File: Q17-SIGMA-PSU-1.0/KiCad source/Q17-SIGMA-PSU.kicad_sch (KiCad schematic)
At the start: 80 parts, among them J1-1 V+ (IN), J1-2 GND, J1-3 V- (IN), J2-1 V+, J2-2 V+, J2-3 GND, J2-4 GND, J2-5 GND, J2-6 V-, J2-7 V-, Q1 BC548B, Q2 BC558B, Q3 BC548B, Q4 BC556B, Q5 BC546B, Q6 IRFZ24NPBF, Q7 IRF9Z34NPBF, Q8 IRFZ24NPBF, Q9 IRF9Z34NPBF, U1 ZHB6792TA, U2 ZHB6792TA

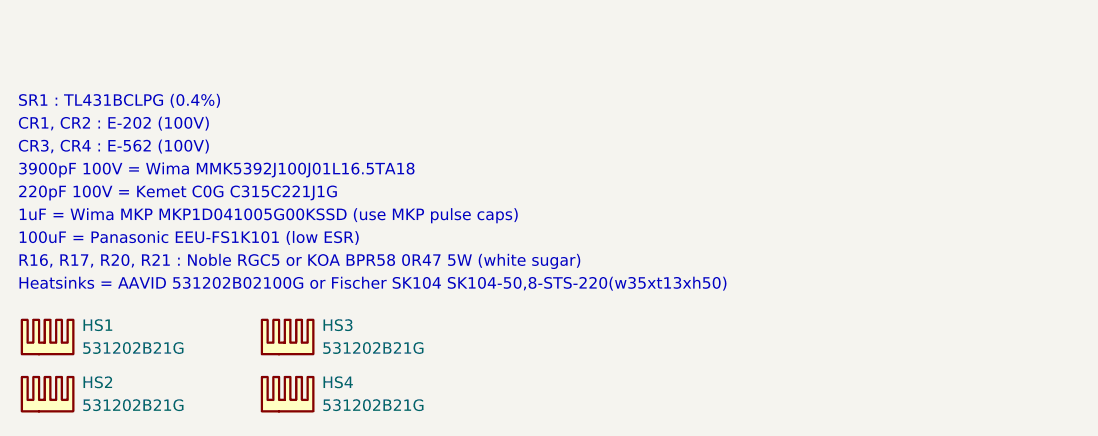
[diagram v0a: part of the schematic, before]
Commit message: Update Q17-SIGMA-PSU.kicad_sch
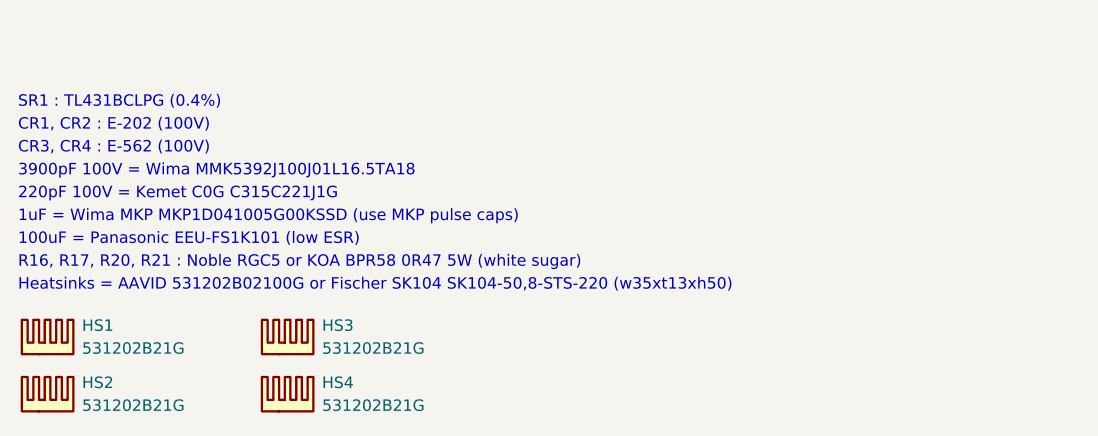
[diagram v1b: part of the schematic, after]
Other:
- note added: "Heatsinks = AAVID 531202B02100G or Fischer SK104 SK104-50,8-STS-220 (w35xt13xh50)"
- note removed: "Heatsinks = AAVID 531202B02100G or Fischer SK104 SK104-50,8-STS-220(w35xt13xh50)"
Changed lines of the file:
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@@
 		(title "Q17-SIGMA Power Supply")
 		(date "2024-04-14")
-		(rev "1.0")
+		(rev "1.0.1")
 		(company "PCB and BOM by stef")
 		(comment 2 "Design and test by Moor")
@@
 		)
 	)
-	(text "Heatsinks = AAVID 531202B02100G or Fischer SK104 SK104-50,8-STS-220(w35xt13xh50)"
+	(text "Heatsinks = AAVID 531202B02100G or Fischer SK104 SK104-50,8-STS-220 (w35xt13xh50)"
 		(exclude_from_sim no)
 		(at 14.478 181.61 0)

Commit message: Q17-SIGMA-PSU-schematic update
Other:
- note added: "All capacitors rated for 80V/100V minimum."
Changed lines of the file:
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@@
 	(title_block
 		(title "Q17-SIGMA Power Supply")
-		(date "2024-04-14")
-		(rev "1.0.1")
+		(date "2024-04-15")
+		(rev "1.0.2")
 		(company "PCB and BOM by stef")
 		(comment 2 "Design and test by Moor")
@@
 		)
 	)
+	(text "All capacitors rated for 80V/100V minimum."
+		(exclude_from_sim no)
+		(at 14.732 158.75 0)
+		(effects
+			(font
+				(size 1.27 1.27)
+			)
+			(justify left)
+		)
+	)
 	(text "1uF = Wima MKP MKP1D041005G00KSSD (use MKP pulse caps)"
 		(exclude_from_sim no)
@@
 		(dnp no)
 		(property "Reference" "R4"
-			(at 110.49 70.358 0)
+			(at 110.49 70.104 0)
 			(effects
 				(font
@@
 		(dnp no)
 		(property "Reference" "R6"
-			(at 119.38 70.358 0)
+			(at 119.38 70.104 0)
 			(effects
 				(font
@@
 		)
 		(property "Value" "510K"
-			(at 119.38 72.136 0)
+			(at 119.38 72.39 0)
 			(effects
 				(font
@@
 		)
 		(property "Value" "100R"
-			(at 215.138 121.158 0)
+			(at 215.138 121.412 0)
 			(effects
 				(font
@@
 		)
 		(property "Value" "100R"
-			(at 202.438 121.158 0)
+			(at 202.438 121.412 0)
 			(effects
 				(font

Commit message: Update Q17-SIGMA-PSU diagram
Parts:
- removed Q6, Q8: IRFZ24NPBF, Package_TO_SOT_THT:TO-220-3_Vertical, symbol Transistor_FET:IRF9540N
- added Q6, Q8: IRFZ24NPBF, Package_TO_SOT_THT:TO-220-3_Vertical, symbol Transistor_FET:IRF540N
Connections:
- net V+ (IN): now also Q6.2 (D), Q8.2 (D)
- net at R10.1: now also Q6.1 (G)
- net at R16.1: now also Q6.3 (S)
- net at R13.1: now also Q8.1 (G)
- net at R17.1: now also Q8.3 (S)
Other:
- note added: "100uF = Panasonic EEU-FS1K101 (low ESR, miniature)"
- note added: "CR1, CR2 : Semitec E-202 (100V)"
- note added: "CR3, CR4 : Semitec E-562 (100V)"
- note added: "Q6, Q8 : IRFZ24NPBF or IRF530NPBF"
- note added: "Q7, Q9 : IRF9Z34NPBF or IRF9540NPBF"
- note removed: "100uF = Panasonic EEU-FS1K101 (low ESR)"
- note removed: "CR1, CR2 : E-202 (100V)"
- note removed: "CR3, CR4 : E-562 (100V)"
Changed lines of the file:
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@@
 		(title "Q17-SIGMA Power Supply")
 		(date "2024-04-15")
-		(rev "1.0.2")
+		(rev "1.0.3")
 		(company "PCB and BOM by stef")
 		(comment 2 "Design and test by Moor")
@@
 		)
 	)
-	(text "100uF = Panasonic EEU-FS1K101 (low ESR)"
+	(text "100uF = Panasonic EEU-FS1K101 (low ESR, miniature)"
 		(exclude_from_sim no)
 		(at 14.478 176.53 0)
@@
 		)
 	)
-	(text "CR3, CR4 : E-562 (100V)"
+	(text "CR3, CR4 : Semitec E-562 (100V)"
 		(exclude_from_sim no)
 		(at 14.478 166.37 0)
@@
 		)
 	)
-	(text "CR1, CR2 : E-202 (100V)"
+	(text "Q7, Q9 : IRF9Z34NPBF or IRF9540NPBF"
+		(exclude_from_sim no)
+		(at 14.732 156.21 0)
+		(effects
+			(font
+				(size 1.27 1.27)
+			)
+			(justify left)
+		)
+	)
+	(text "CR1, CR2 : Semitec E-202 (100V)"
 		(exclude_from_sim no)
 		(at 14.478 163.83 0)
@@
 		)
 	)
+	(text "Q6, Q8 : IRFZ24NPBF or IRF530NPBF"
+		(exclude_from_sim no)
+		(at 14.732 153.67 0)
+		(effects
+			(font
+				(size 1.27 1.27)
+			)
+			(justify left)
+		)
+	)
 	(text "220pF 100V = Kemet C0G C315C221J1G "
 		(exclude_from_sim no)
@@
 	)
 	(symbol
+		(lib_id "Transistor_FET:IRF540N")
+		(at 213.36 53.34 90)
+		(unit 1)
+		(exclude_from_sim no)
+		(in_bom yes)
+		(on_board yes)
+		(dnp no)
+		(fields_autoplaced yes)
+		(property "Reference" "Q8"
+			(at 213.36 44.45 90)
+			(effects
+				(font
+					(size 1.27 1.27)
+				)
+			)
+		)
+		(property "Value" "IRFZ24NPBF"
+			(at 213.36 46.99 90)
+			(effects
+				(font
+					(size 1.27 1.27)
+				)
+			)
+		)
+		(property "Footprint" "Package_TO_SOT_THT:TO-220-3_Vertical"
+			(at 215.265 48.26 0)
+			(effects
+				(font
+					(size 1.27 1.27)
+					(italic yes)
+				)
+				(justify left)
+				(hide yes)
+			)
+		)
+		(property "Datasheet" "https://www.mouser.fr/datasheet/2/196/Infineon_IRFZ24N_DataSheet_v01_01_EN-3363353.pdf"
+			(at 217.17 48.26 0)
+			(effects
+				(font
+					(size 1.27 1.27)
+				)
+				(justify left)
+				(hide yes)
+			)
+		)
+		(property "Description" "MOSFET MOSFT 55V 17A 70mOhm 13.3nC"
+			(at 213.36 53.34 0)
+			(effects
+				(font
+					(size 1.27 1.27)
+				)
+				(hide yes)
+			)
+		)
+		(property "Part#" "IRFZ24NPBF"
+			(at 213.36 53.34 0)
+			(effects
+				(font
+					(size 1.27 1.27)
+				)
+				(hide yes)
+			)
+		)
+		(property "Mouser" "942-IRFZ24NPBF"
+			(at 213.36 53.34 0)
+			(effects
+				(font
+					(size 1.27 1.27)
+				)
+				(hide yes)
+			)
+		)
+		(pin "1"
+		)
+		(pin "2"
+		)
+		(pin "3"
+		)
+		(instances
+			(project "Q17-SIGMA-PSU"
+				(path "/6f6e3082-536f-4dd6-9db0-4603443bd8a6"
+					(reference "Q8")
+					(unit 1)
+				)
+			)
+		)
+	)
+	(symbol
 		(lib_id "Device:C_Polarized")
 		(at 96.52 78.74 0)
@@
 	)
 	(symbol
-		(lib_id "Transistor_FET:IRF9540N")
-		(at 200.66 41.91 90)
-		(unit 1)
-		(exclude_from_sim no)
-		(in_bom yes)
-		(on_board yes)
-		(dnp no)
-		(fields_autoplaced yes)
-		(property "Reference" "Q6"
-			(at 200.66 33.02 90)
-			(effects
-				(font
-					(size 1.27 1.27)
-				)
-			)
-		)
-		(property "Value" "IRFZ24NPBF"
-			(at 200.66 35.56 90)
-			(effects
-				(font
-					(size 1.27 1.27)
-				)
-			)
-		)
-		(property "Footprint" "Package_TO_SOT_THT:TO-220-3_Vertical"
-			(at 202.565 36.83 0)
-			(effects
-				(font
-					(size 1.27 1.27)
-					(italic yes)
-				)
-				(justify left)
-				(hide yes)
-			)
-		)
-		(property "Datasheet" "https://www.mouser.fr/datasheet/2/196/Infineon_IRFZ24N_DataSheet_v01_01_EN-3363353.pdf"
-			(at 204.47 36.83 0)
-			(effects
-				(font
-					(size 1.27 1.27)
-				)
-				(justify left)
-				(hide yes)
-			)
-		)
-		(property "Description" "MOSFET MOSFT 55V 17A 70mOhm 13.3nC"
-			(at 200.66 41.91 0)
-			(effects
-				(font
-					(size 1.27 1.27)
-				)
-				(hide yes)
-			)
-		)
-		(property "Part#" "IRFZ24NPBF"
-			(at 200.66 41.91 90)
-			(effects
-				(font
-					(size 1.27 1.27)
-				)
-				(hide yes)
-			)
-		)
-		(property "Mouser" "942-IRFZ24NPBF"
-			(at 200.66 41.91 90)
-			(effects
-				(font
-					(size 1.27 1.27)
-				)
-				(hide yes)
-			)
-		)
-		(pin "2"
-		)
-		(pin "1"
-		)
-		(pin "3"
-		)
-		(instances
-			(project "Q17-SIGMA-PSU"
-				(path "/6f6e3082-536f-4dd6-9db0-4603443bd8a6"
-					(reference "Q6")
-					(unit 1)
-				)
-			)
-		)
-	)
-	(symbol
 		(lib_id "Device:C_Polarized")
 		(at 96.52 105.41 0)
@@
 			)
 		)
-		(property "Datasheet" "https://www.mouser.fr/datasheet/2/268/LDS_0159-1593968.pdf"
+		(property "Datasheet" "https://www.mouser.fr/datasheet/2/362/P22-23-CRD-1729293.pdf"
 			(at 185.42 97.79 0)
 			(effects
@@
 		)
 		(property "Value" "100R"
-			(at 215.138 121.412 0)
+			(at 215.138 122.174 0)
 			(effects
 				(font
@@
 		)
 		(property "Value" "100R"
-			(at 202.438 121.412 0)
+			(at 202.438 122.174 0)
 			(effects
 				(font
@@
 	)
 	(symbol
-		(lib_id "Transistor_FET:IRF9540N")
-		(at 213.36 53.34 90)
-		(unit 1)
-		(exclude_from_sim no)
-		(in_bom yes)
-		(on_board yes)
-		(dnp no)
-		(fields_autoplaced yes)
-		(property "Reference" "Q8"
-			(at 213.36 44.45 90)
-			(effects
-				(font
-					(size 1.27 1.27)
-				)
-			)
-		)
-		(property "Value" "IRFZ24NPBF"
-			(at 213.36 46.99 90)
-			(effects
-				(font
-					(size 1.27 1.27)
-				)
-			)
-		)
-		(property "Footprint" "Package_TO_SOT_THT:TO-220-3_Vertical"
-			(at 215.265 48.26 0)
-			(effects
-				(font
-					(size 1.27 1.27)
-					(italic yes)
-				)
-				(justify left)
-				(hide yes)
-			)
-		)
-		(property "Datasheet" "https://www.mouser.fr/datasheet/2/196/Infineon_IRFZ24N_DataSheet_v01_01_EN-3363353.pdf"
-			(at 217.17 48.26 0)
-			(effects
-				(font
-					(size 1.27 1.27)
-				)
-				(justify left)
-				(hide yes)
-			)
-		)
-		(property "Description" "MOSFET MOSFT 55V 17A 70mOhm 13.3nC"
-			(at 213.36 53.34 0)
-			(effects
-				(font
-					(size 1.27 1.27)
-				)
-				(hide yes)
-			)
-		)
-		(property "Part#" "IRFZ24NPBF"
-			(at 213.36 53.34 90)
-			(effects
-				(font
-					(size 1.27 1.27)
-				)
-				(hide yes)
-			)
-		)
-		(property "Mouser" "942-IRFZ24NPBF"
-			(at 213.36 53.34 90)
-			(effects
-				(font
-					(size 1.27 1.27)
-				)
-				(hide yes)
-			)
-		)
-		(pin "2"
-		)
-		(pin "1"
-		)
-		(pin "3"
-		)
-		(instances
-			(project "Q17-SIGMA-PSU"
-				(path "/6f6e3082-536f-4dd6-9db0-4603443bd8a6"
-					(reference "Q8")
-					(unit 1)
-				)
-			)
-		)
-	)
-	(symbol
 		(lib_id "Device:C")
 		(at 49.53 118.11 0)
@@
 	)
 	(symbol
+		(lib_id "Transistor_FET:IRF540N")
+		(at 200.66 41.91 90)
+		(unit 1)
+		(exclude_from_sim no)
+		(in_bom yes)
+		(on_board yes)
+		(dnp no)
+		(fields_autoplaced yes)
+		(property "Reference" "Q6"
+			(at 200.66 33.02 90)
+			(effects
+				(font
+					(size 1.27 1.27)
+				)
+			)
+		)
+		(property "Value" "IRFZ24NPBF"
+			(at 200.66 35.56 90)
+			(effects
+				(font
+					(size 1.27 1.27)
+				)
+			)
+		)
+		(property "Footprint" "Package_TO_SOT_THT:TO-220-3_Vertical"
+			(at 202.565 36.83 0)
+			(effects
+				(font
+					(size 1.27 1.27)
+					(italic yes)
+				)
+				(justify left)
+				(hide yes)
+			)
+		)
+		(property "Datasheet" "https://www.mouser.fr/datasheet/2/196/Infineon_IRFZ24N_DataSheet_v01_01_EN-3363353.pdf"
+			(at 204.47 36.83 0)
+			(effects
+				(font
+					(size 1.27 1.27)
+				)
+				(justify left)
+				(hide yes)
+			)
+		)
+		(property "Description" "MOSFET MOSFT 55V 17A 70mOhm 13.3nC"
+			(at 200.66 41.91 0)
+			(effects
+				(font
+					(size 1.27 1.27)
+				)
+				(hide yes)
+			)
+		)
+		(property "Part#" "IRFZ24NPBF"
+			(at 200.66 41.91 0)
+			(effects
+				(font
+					(size 1.27 1.27)
+				)
+				(hide yes)
+			)
+		)
+		(property "Mouser" "942-IRFZ24NPBF"
+			(at 200.66 41.91 0)
+			(effects
+				(font
+					(size 1.27 1.27)
+				)
+				(hide yes)
+			)
+		)
+		(pin "1"
+		)
+		(pin "2"
+		)
+		(pin "3"
+		)
+		(instances
+			(project "Q17-SIGMA-PSU"
+				(path "/6f6e3082-536f-4dd6-9db0-4603443bd8a6"
+					(reference "Q6")
+					(unit 1)
+				)
+			)
+		)
+	)
+	(symbol
 		(lib_id "Diode:1N4148")
 		(at 185.42 85.09 90)
@@
 			)
 		)
-		(property "Datasheet" "https://www.mouser.fr/datasheet/2/268/LDS_0159-1593968.pdf"
+		(property "Datasheet" "https://www.mouser.fr/datasheet/2/362/P22-23-CRD-1729293.pdf"
 			(at 185.42 85.09 0)
 			(effects

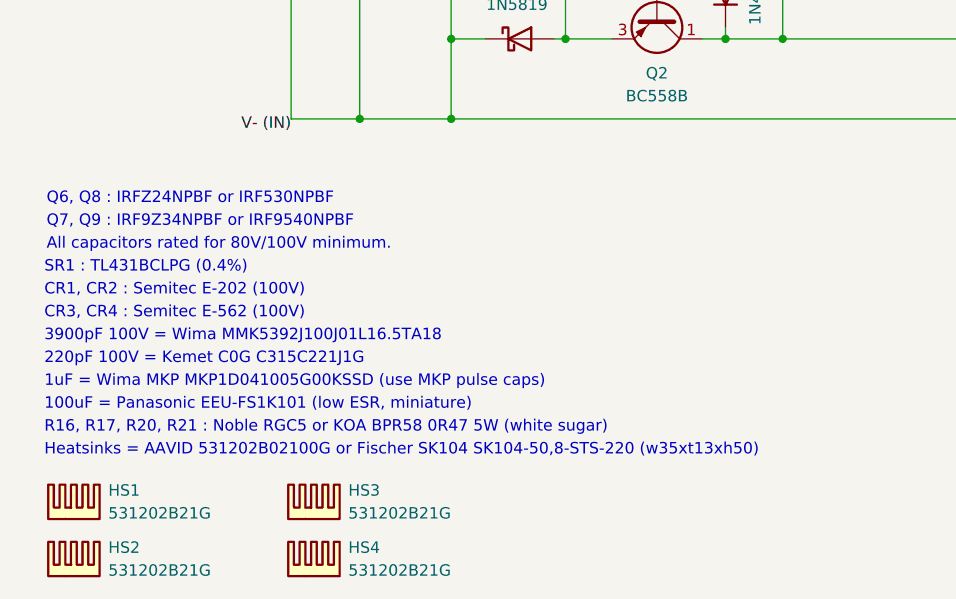
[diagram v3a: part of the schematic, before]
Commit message: Q17-SIGMA-PSU-schematic
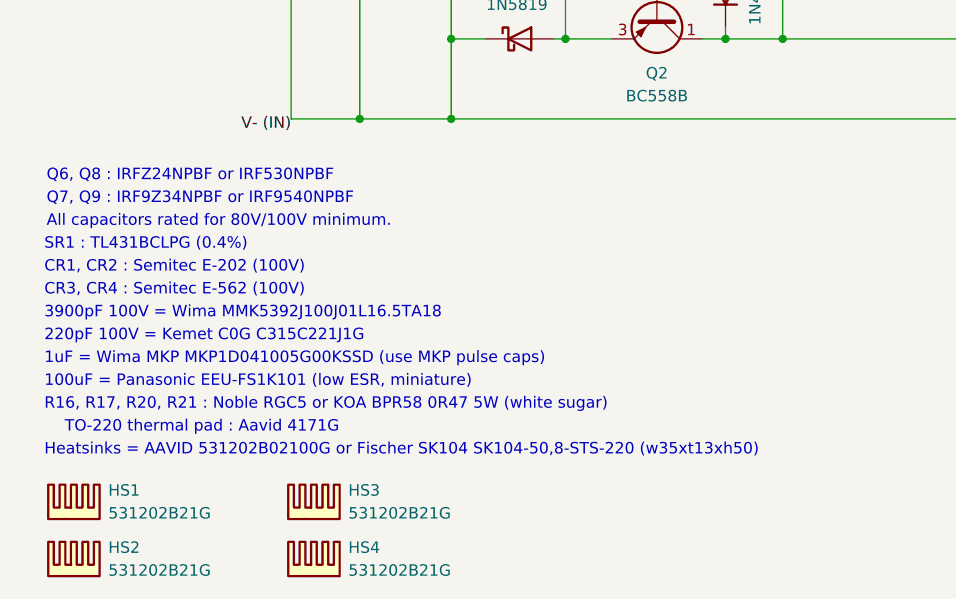
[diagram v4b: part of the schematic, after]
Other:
- note added: "TO-220 thermal pad : Aavid 4171G"
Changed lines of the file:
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@@
 	(title_block
 		(title "Q17-SIGMA Power Supply")
-		(date "2024-04-15")
-		(rev "1.0.3")
+		(date "2024-04-17")
+		(rev "1.0.4")
 		(company "PCB and BOM by stef")
 		(comment 2 "Design and test by Moor")
@@
 	(text "All capacitors rated for 80V/100V minimum."
 		(exclude_from_sim no)
-		(at 14.732 158.75 0)
+		(at 14.732 156.21 0)
 		(effects
 			(font
@@
 	)
 	(text "1uF = Wima MKP MKP1D041005G00KSSD (use MKP pulse caps)"
+		(exclude_from_sim no)
+		(at 14.478 171.45 0)
+		(effects
+			(font
+				(size 1.27 1.27)
+			)
+			(justify left)
+		)
+	)
+	(text "SR1 : TL431BCLPG (0.4%)"
+		(exclude_from_sim no)
+		(at 14.478 158.75 0)
+		(effects
+			(font
+				(size 1.27 1.27)
+			)
+			(justify left)
+		)
+	)
+	(text "100uF = Panasonic EEU-FS1K101 (low ESR, miniature)"
 		(exclude_from_sim no)
 		(at 14.478 173.99 0)
@@
 		)
 	)
-	(text "SR1 : TL431BCLPG (0.4%)"
+	(text "TO-220 thermal pad : Aavid 4171G"
+		(exclude_from_sim no)
+		(at 32.004 179.07 0)
+		(effects
+			(font
+				(size 1.27 1.27)
+			)
+		)
+	)
+	(text "3900pF 100V = Wima MMK5392J100J01L16.5TA18"
+		(exclude_from_sim no)
+		(at 14.478 166.37 0)
+		(effects
+			(font
+				(size 1.27 1.27)
+			)
+			(justify left)
+		)
+	)
+	(text "CR3, CR4 : Semitec E-562 (100V)"
+		(exclude_from_sim no)
+		(at 14.478 163.83 0)
+		(effects
+			(font
+				(size 1.27 1.27)
+			)
+			(justify left)
+		)
+	)
+	(text "R16, R17, R20, R21 : Noble RGC5 or KOA BPR58 0R47 5W (white sugar)"
+		(exclude_from_sim no)
+		(at 14.478 176.53 0)
+		(effects
+			(font
+				(size 1.27 1.27)
+			)
+			(justify left)
+		)
+	)
+	(text "Q7, Q9 : IRF9Z34NPBF or IRF9540NPBF"
+		(exclude_from_sim no)
+		(at 14.732 153.67 0)
+		(effects
+			(font
+				(size 1.27 1.27)
+			)
+			(justify left)
+		)
+	)
+	(text "CR1, CR2 : Semitec E-202 (100V)"
 		(exclude_from_sim no)
 		(at 14.478 161.29 0)
@@
 		)
 	)
-	(text "100uF = Panasonic EEU-FS1K101 (low ESR, miniature)"
+	(text "Q6, Q8 : IRFZ24NPBF or IRF530NPBF"
 		(exclude_from_sim no)
-		(at 14.478 176.53 0)
+		(at 14.732 151.13 0)
 		(effects
 			(font
@@
 		)
 	)
-	(text "3900pF 100V = Wima MMK5392J100J01L16.5TA18"
+	(text "220pF 100V = Kemet C0G C315C221J1G "
 		(exclude_from_sim no)
 		(at 14.478 168.91 0)
 		(effects
 			(font
-				(size 1.27 1.27)
-			)
-			(justify left)
-		)
-	)
-	(text "CR3, CR4 : Semitec E-562 (100V)"
-		(exclude_from_sim no)
-		(at 14.478 166.37 0)
-		(effects
-			(font
-				(size 1.27 1.27)
-			)
-			(justify left)
-		)
-	)
-	(text "R16, R17, R20, R21 : Noble RGC5 or KOA BPR58 0R47 5W (white sugar)"
-		(exclude_from_sim no)
-		(at 14.478 179.07 0)
-		(effects
-			(font
-				(size 1.27 1.27)
-			)
-			(justify left)
-		)
-	)
-	(text "Q7, Q9 : IRF9Z34NPBF or IRF9540NPBF"
-		(exclude_from_sim no)
-		(at 14.732 156.21 0)
-		(effects
-			(font
-				(size 1.27 1.27)
-			)
-			(justify left)
-		)
-	)
-	(text "CR1, CR2 : Semitec E-202 (100V)"
-		(exclude_from_sim no)
-		(at 14.478 163.83 0)
-		(effects
-			(font
-				(size 1.27 1.27)
-			)
-			(justify left)
-		)
-	)
-	(text "Q6, Q8 : IRFZ24NPBF or IRF530NPBF"
-		(exclude_from_sim no)
-		(at 14.732 153.67 0)
-		(effects
-			(font
-				(size 1.27 1.27)
-			)
-			(justify left)
-		)
-	)
-	(text "220pF 100V = Kemet C0G C315C221J1G "
-		(exclude_from_sim no)
-		(at 14.478 171.45 0)
-		(effects
-			(font

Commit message: Q17-SIGMA-PSU-schematic update
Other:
- note added: "3900pF 100V = Kemet MMK5392J100J01L16.5TA18 or Kemet PHE426DJ4390JR05"
- note removed: "3900pF 100V = Wima MMK5392J100J01L16.5TA18"
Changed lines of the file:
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@@
 	(title_block
 		(title "Q17-SIGMA Power Supply")
-		(date "2024-04-17")
-		(rev "1.0.4")
+		(date "2024-04-20")
+		(rev "1.0.5")
 		(company "PCB and BOM by stef")
 		(comment 2 "Design and test by Moor")
@@
 		)
 	)
-	(text "3900pF 100V = Wima MMK5392J100J01L16.5TA18"
+	(text "3900pF 100V = Kemet MMK5392J100J01L16.5TA18 or Kemet PHE426DJ4390JR05"
 		(exclude_from_sim no)
 		(at 14.478 166.37 0)
